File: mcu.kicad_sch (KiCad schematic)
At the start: 66 parts, among them J10 PinHeader_2x10_P1.27mm_SMD_Sh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, SW5 SW_B3U-1000P_SMD, SW6 CAS-120TA, U1 STM32H753ZIT6, Y1 Resonator_32.768kHz_ECX-31B, Y2 Oscillator_25MHz_ESC_2016MV

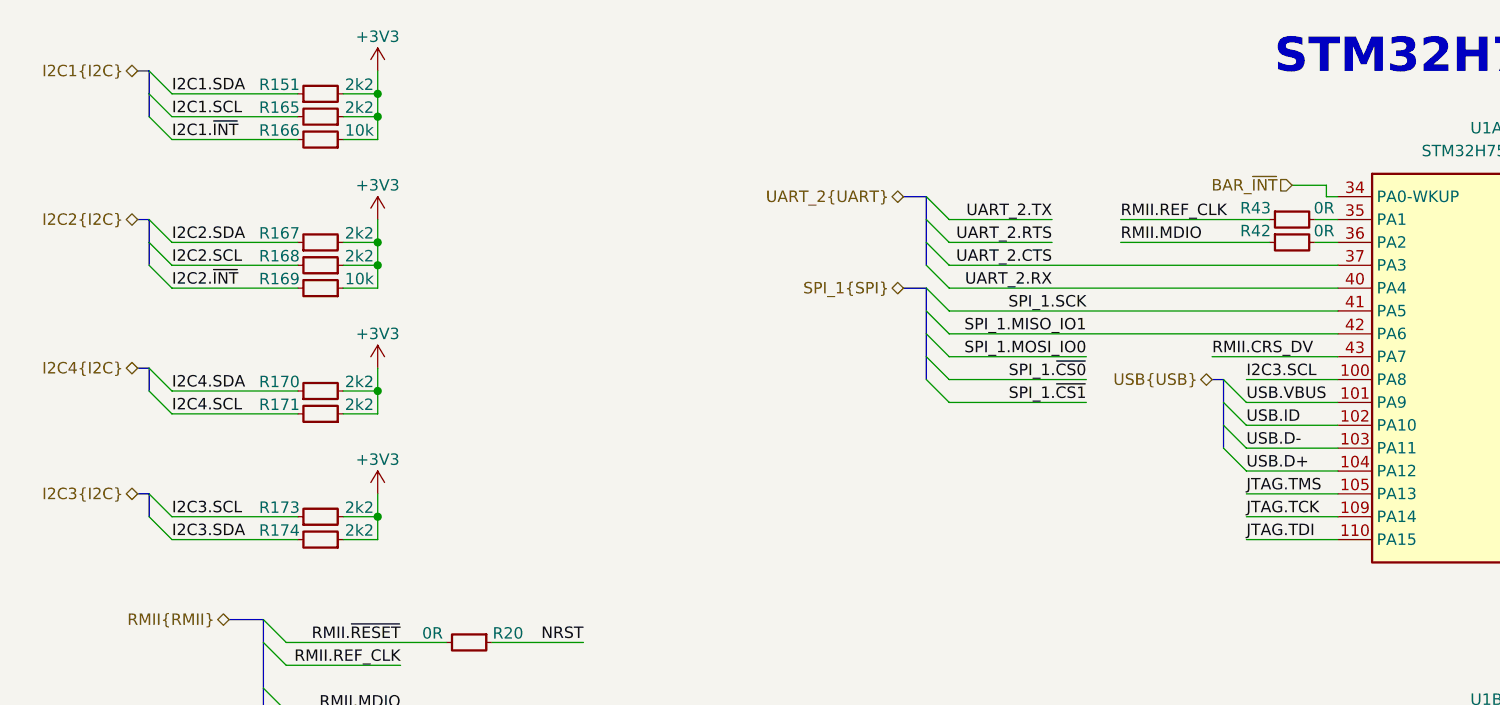
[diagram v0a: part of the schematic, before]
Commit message: [#95036] Fix MCU pin attachment
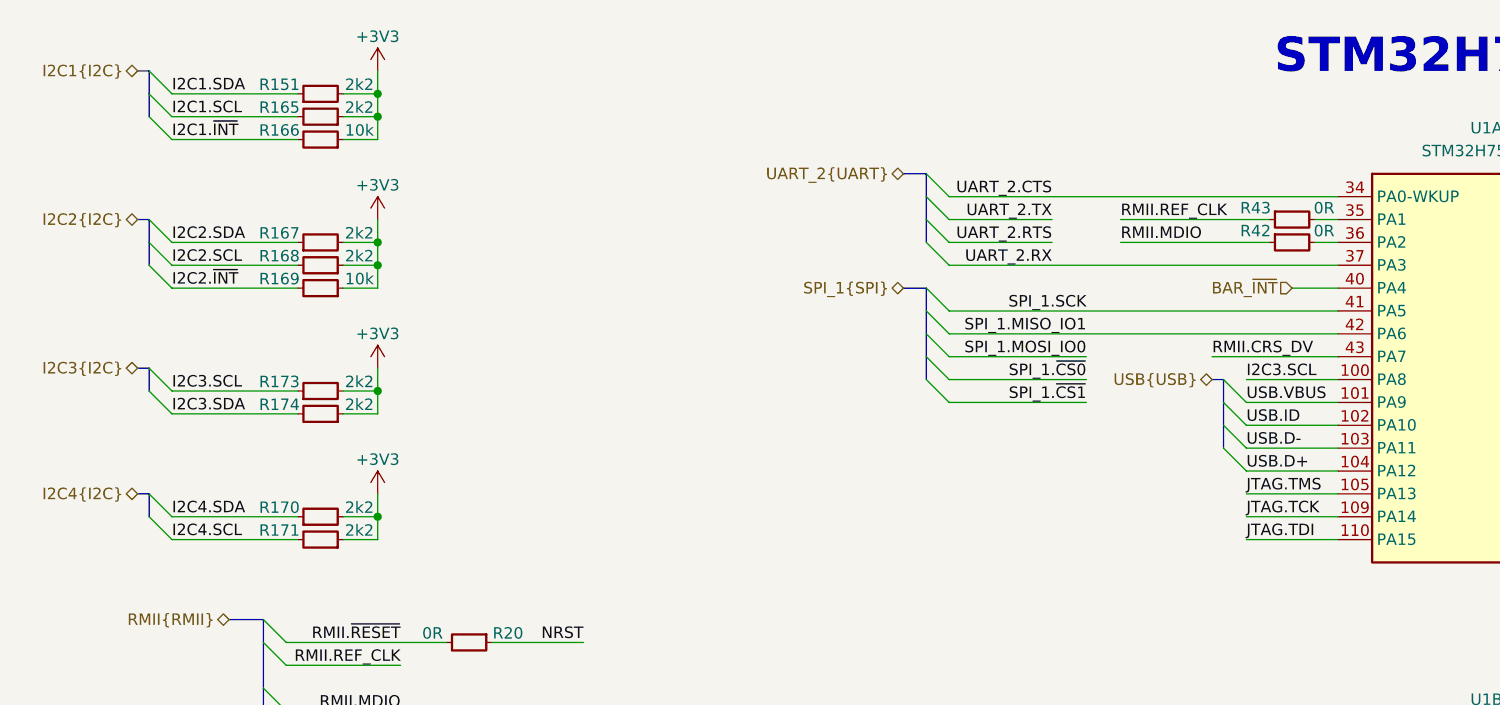
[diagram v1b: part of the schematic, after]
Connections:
- net BAR_~{INT}: now also U1.40 (PA4); no longer U1.34 (PA0-WKUP)
- net UART_2.CTS: now also U1.34 (PA0-WKUP); no longer U1.37 (PA3)
- net UART_2.RX: now also U1.37 (PA3); no longer U1.40 (PA4)
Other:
- moved on the sheet: R170, R171, R173, R174

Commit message: [#95398] Cleanup
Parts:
- removed R170, R171, R173, R174: R_2k2_0402, antmicro-footprints:R_0402_1005Metric, symbol antmicroResistors0402:R_2k2_0402
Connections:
- net EN_PMOD: no longer names the net of U1.113 (PC12)
- net EN_RPI_CONN: no longer names the net of U1.48 (PB2)
- net GPIO0: no longer names the net of U1.141 (PE0)
- net GPIO1: no longer names the net of U1.142 (PE1)
- net GPIO12: no longer names the net of U1.60 (PE9)
- net GPIO13: no longer names the net of U1.64 (PE11)
- net GPIO16: no longer names the net of U1.63 (PE10)
- net GPIO17: no longer names the net of U1.65 (PE12)
- net GPIO18: no longer names the net of U1.66 (PE13)
- net GPIO19: no longer names the net of U1.67 (PE14)
- net GPIO20: no longer names the net of U1.68 (PE15)
- net GPIO21: no longer names the net of U1.13 (PF3)
- net GPIO22: no longer names the net of U1.14 (PF4)
- net GPIO23: no longer names the net of U1.15 (PF5)
- net GPIO24: no longer names the net of U1.50 (PF12)
- net GPIO25: no longer names the net of U1.56 (PG0)
- net GPIO26: no longer names the net of U1.57 (PG1)
- net GPIO27: no longer names the net of U1.87 (PG2)
- net GPIO4: no longer names the net of U1.96 (PC6)
- net GPIO5: no longer names the net of U1.58 (PE7)
- net GPIO6: no longer names the net of U1.59 (PE8)
- net I2C3.SCL: no longer names the net of U1.100 (PA8)
- net I2C3.SDA: no longer names the net of U1.99 (PC9)
- net I2C4.SCL: no longer names the net of U1.54 (PF14)
- net I2C4.SDA: no longer names the net of U1.55 (PF15)
- net PMOD1_IO5: no longer names the net of U1.139 (PB8)
- net PMOD1_IO6: no longer names the net of U1.129 (PG14)
- net PMOD1_IO7: no longer names the net of U1.132 (PG15)
- net PMOD1_IO8: no longer names the net of U1.140 (PB9)
- net PMOD2_IO5: no longer names the net of U1.90 (PG5)
- net PMOD2_IO6: no longer names the net of U1.91 (PG6)
- net PMOD2_IO6: no longer U1.46 (PB0)
- net SPI_1.MISO_IO1: no longer names the net of U1.42 (PA6)
- net SPI_1.MOSI_IO0: no longer names the net of U1.123 (PD7)
- net SPI_1.SCK: no longer names the net of U1.41 (PA5)
- net SPI_1.~{CS0}: no longer names the net of U1.111 (PC10)
- net SPI_1.~{CS1}: no longer names the net of U1.112 (PC11)
- net SPI_2.MISO_IO1: no longer names the net of U1.28 (PC2_C)
- net SPI_2.MOSI_IO0: no longer names the net of U1.29 (PC3_C)
- net SPI_2.~{CS0}: no longer names the net of U1.26 (PC0)
- net UART1.RX: no longer names the net of U1.76 (PB15)
- net UART1.TX: no longer names the net of U1.75 (PB14)
- net UART_3.CTS: no longer names the net of U1.80 (PD11)
- net UART_3.RTS: no longer names the net of U1.81 (PD12)
- net UART_3.RX: no longer names the net of U1.78 (PD9)
- net UART_3.TX: no longer names the net of U1.77 (PD8)

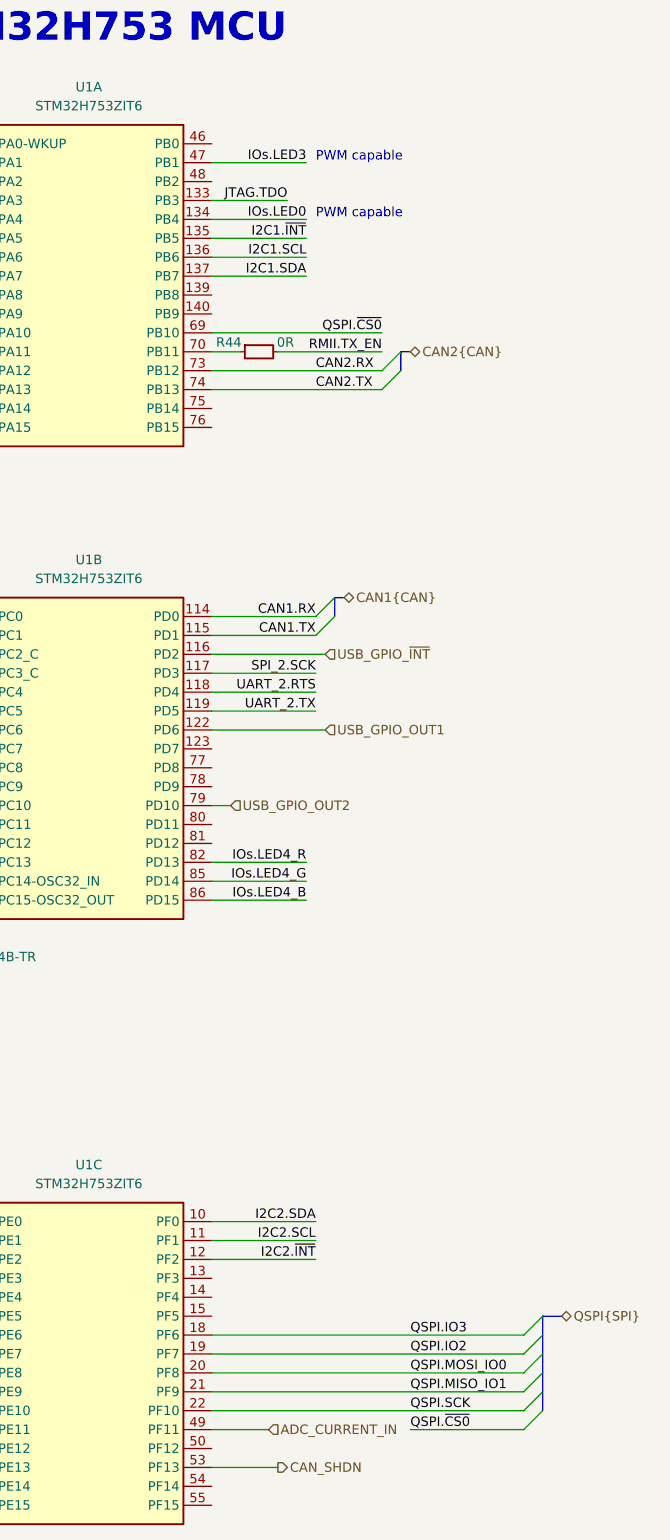
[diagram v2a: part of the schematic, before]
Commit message: [#95398] Connect potentiometers
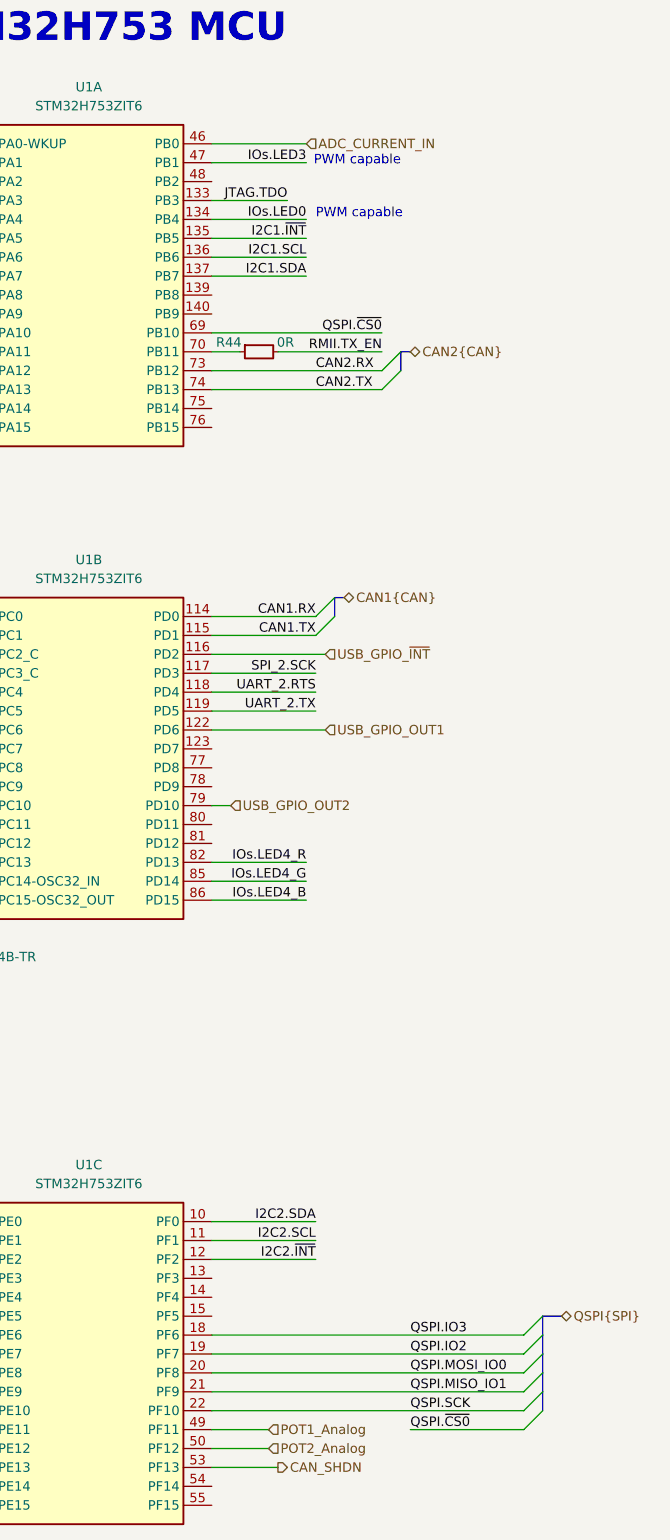
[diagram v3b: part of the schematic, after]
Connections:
- net ADC_CURRENT_IN: now also U1.46 (PB0); no longer U1.49 (PF11)
- net POT2_Analog: now reaches U1.50 (PF12)
- new net POT1_Analog: U1.49 (PF11)
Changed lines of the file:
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@@
 	(text "PWM capable"
 		(exclude_from_sim no)
-		(at 215.392 41.148 0)
+		(at 215.138 41.656 0)
 		(effects
 			(font
@@
 	(wire
 		(pts
+			(xy 195.58 39.37) (xy 208.28 39.37)
+		)
+		(stroke
+			(width 0)
+			(type default)
+		)
+	)
+	(wire
+		(pts
 			(xy 55.88 25.4) (xy 55.88 27.94)
 		)
@@
 	(wire
 		(pts
+			(xy 195.58 214.63) (xy 203.2 214.63)
+		)
+		(stroke
+			(width 0)
+			(type default)
+		)
+	)
+	(wire
+		(pts
 			(xy 317.5 214.63) (xy 313.69 214.63)
 		)
@@
 	(hierarchical_label "ADC_CURRENT_IN"
 		(shape input)
-		(at 203.2 212.09 0)
+		(at 208.28 39.37 0)
 		(effects
 			(font
@@
 		)
 	)
+	(hierarchical_label "POT2_Analog"
+		(shape input)
+		(at 203.2 214.63 0)
+		(effects
+			(font
+				(size 1.27 1.27)
+			)
+			(justify left)
+		)
+	)
 	(hierarchical_label "USB_GPIO_OUT2"
 		(shape input)
@@
 		)
 	)
+	(hierarchical_label "POT1_Analog"
+		(shape input)
+		(at 203.2 212.09 0)
+		(effects
+			(font
+				(size 1.27 1.27)
+			)
+			(justify left)
+		)
+	)

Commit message: [#95398] Schematic cleanup
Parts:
- removed R169: R_10k_0402, antmicro-footprints:R_0402_1005Metric, symbol antmicroResistors0402:R_10k_0402
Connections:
- net +3V3: now also R151.1, R165.2, R166.2, R168.2; no longer R151.2, R165.1, R166.1, R168.1
- net I2C1.SCL: now also R165.1; no longer R165.2
- net I2C1.SDA: now also R151.2; no longer R151.1
- net I2C1.~{INT}: now also R166.1; no longer R166.2
- net I2C2.SCL: now also R167.1; no longer R168.2
- net I2C2.SDA: now also R168.1; no longer R167.1
- net I2C2.~{INT}: no longer names the net of U1.12 (PF2)
- no-connect marks 2 -> 44
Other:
- moved on the sheet: R11, R12, R151, R165, R166, R167, R168

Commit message: [#95398] Clear ERC
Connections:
- net SPI_2.SCK: no longer names the net of U1.117 (PD3)
- no-connect marks 44 -> 48
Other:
- moved on the sheet: C24, C25, D6, D7, R17, R18, R19, SW5, SW6, Y2
